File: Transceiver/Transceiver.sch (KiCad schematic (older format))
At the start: 8 parts, among them J1 Conn_02x05, J2 Conn_02x20, J3 Conn_02x20, J4 Conn_02x05, J5 MountingHole, J6 MountingHole, J7 MountingHole, J8 MountingHole

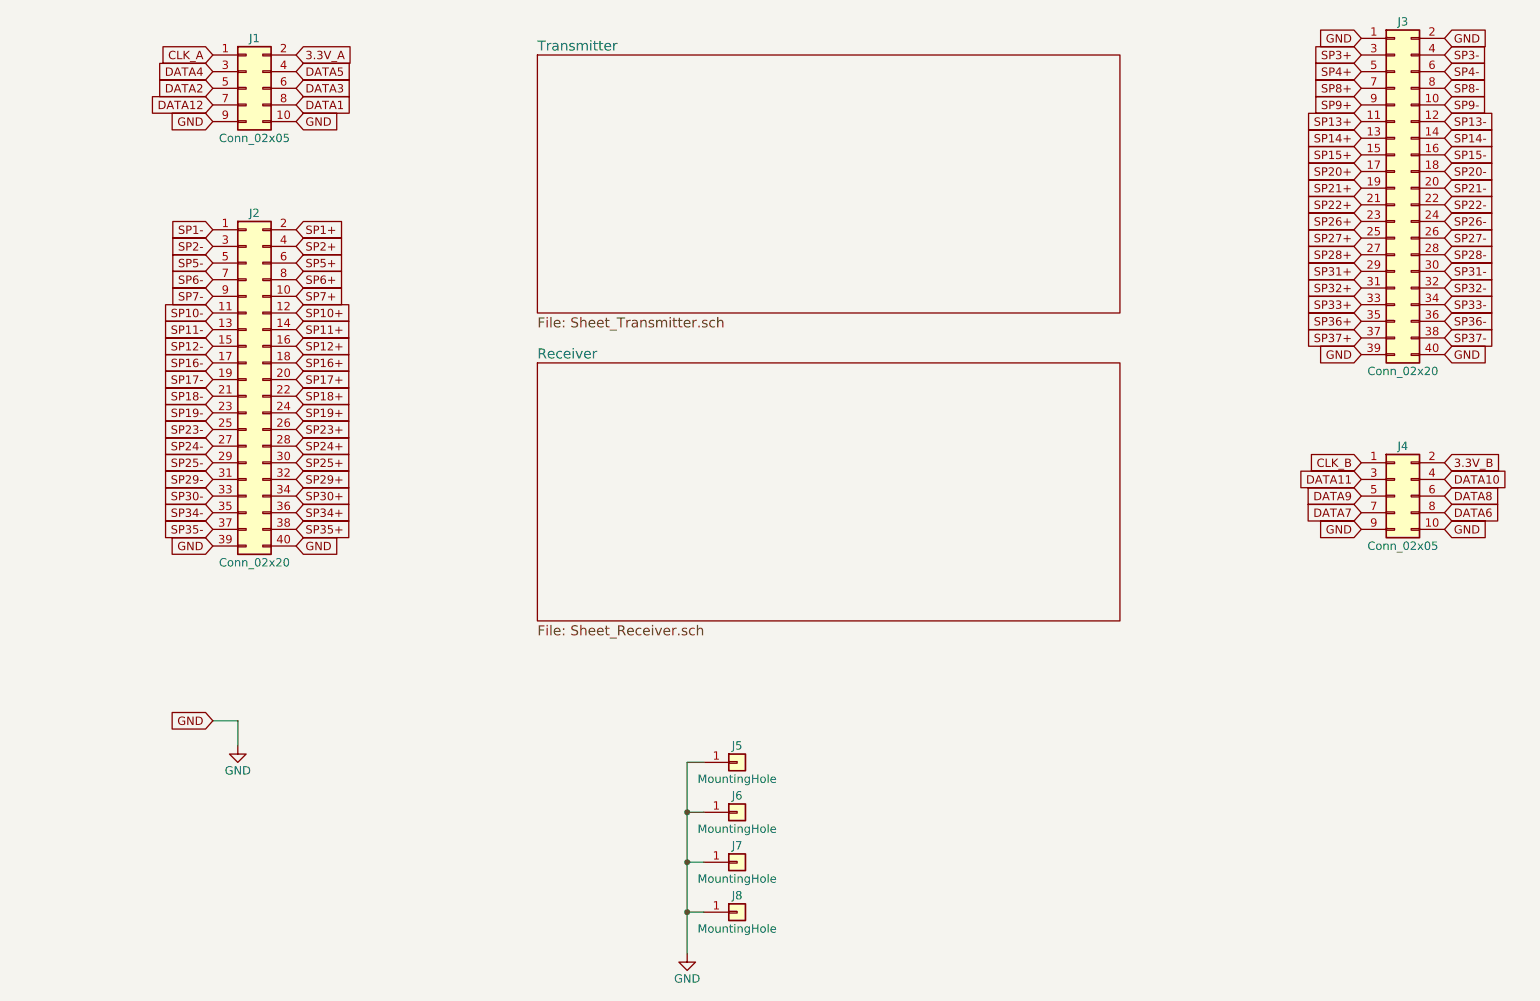
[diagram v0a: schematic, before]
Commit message: トランシーバ基板にLEDとIMUを追加
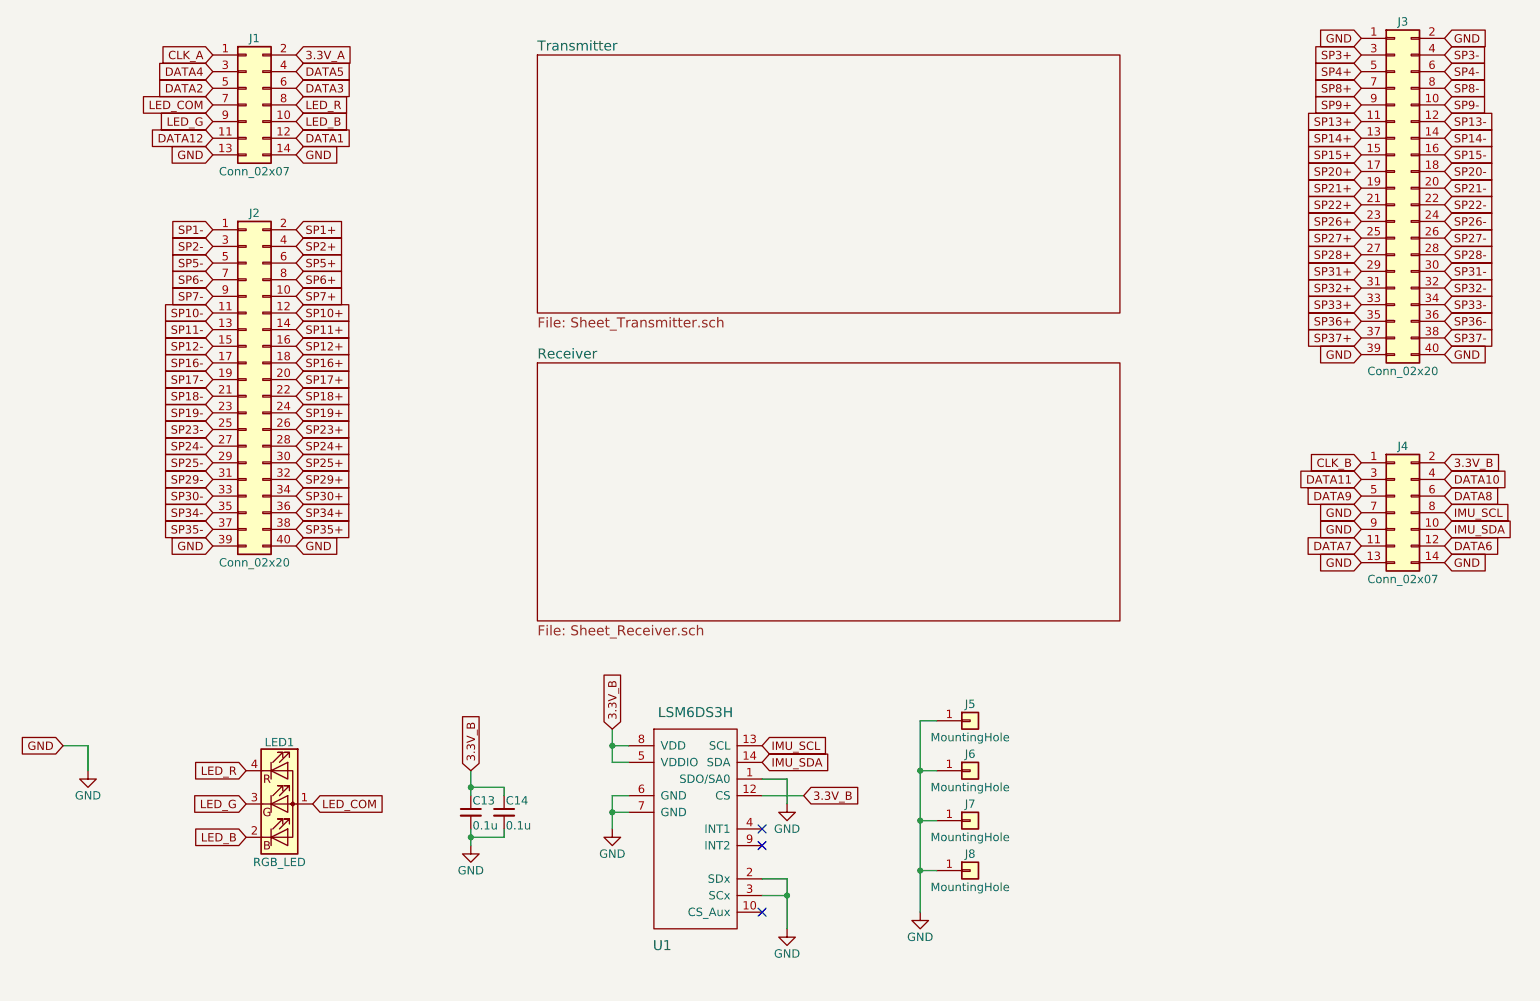
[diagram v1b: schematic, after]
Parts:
- removed J1, J4: Conn_02x05, Pin_Headers:Pin_Header_Straight_2x05_Pitch2.54mm, symbol Conn_02x05_Odd_Even
- added C13, C14: 0.1u, Capacitors_SMD:C_0603_HandSoldering, symbol C_Small
- added J1, J4: Conn_02x07, Pin_Headers:Pin_Header_Straight_2x07_Pitch2.54mm, symbol Conn_02x07_Odd_Even
- added LED1: RGB_LED, LEDs:LED_Cree-PLCC4_2x2mm_CW, symbol RGB_LED
- added U1: LSM6DS3H, Housings_LGA:Bosch_LGA-14_3x2.5mm_Pitch0.5mm, symbol LSM6DS3H
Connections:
- net 3.3V_A: now also J1.2 (Pin_2)
- net 3.3V_B: now also C13.1, C14.1, J4.2 (Pin_2), U1.12 (CS), U1.5 (VDDIO), U1.8 (VDD)
- net CLK_A: now also J1.1 (Pin_1)
- net CLK_B: now also J4.1 (Pin_1)
- net DATA1: now also J1.12 (Pin_12)
- net DATA10: now also J4.4 (Pin_4)
- net DATA11: now also J4.3 (Pin_3)
- net DATA12: now also J1.11 (Pin_11)
- net DATA2: now also J1.5 (Pin_5)
- net DATA3: now also J1.6 (Pin_6)
- net DATA4: now also J1.3 (Pin_3)
- net DATA5: now also J1.4 (Pin_4)
- net DATA6: now also J4.12 (Pin_12)
- net DATA7: now also J4.11 (Pin_11)
- net DATA8: now also J4.6 (Pin_6)
- net DATA9: now also J4.5 (Pin_5)
- net GND: now also C13.2, C14.2, J1.13 (Pin_13), J1.14 (Pin_14), J4.13 (Pin_13), J4.14 (Pin_14), J4.7 (Pin_7), J4.9 (Pin_9), U1.1 (SDO/SA0), U1.2 (SDx), U1.3 (SCx), U1.6 (GND), U1.7 (GND)
- new net IMU_SCL: J4.8 (Pin_8), U1.13 (SCL)
- new net IMU_SDA: J4.10 (Pin_10), U1.14 (SDA)
- new net LED_B: J1.10 (Pin_10), LED1.2 (BK)
- new net LED_COM: J1.7 (Pin_7), LED1.1 (A)
- new net LED_G: J1.9 (Pin_9), LED1.3 (GK)
- new net LED_R: J1.8 (Pin_8), LED1.4 (RK)
- no-connect marks 0 -> 3
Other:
- moved on the sheet: J5, J6, J7, J8
